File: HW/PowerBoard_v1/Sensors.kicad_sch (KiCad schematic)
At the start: 46 parts, among them U3 MCP9700AT-ETT, U4 PAMC1350DWVR, U5 PAMC1350DWVR, U6 PAMC1350DWVR, U7 PAMC1350DWVR, U8 3v3 ISO DC/DC

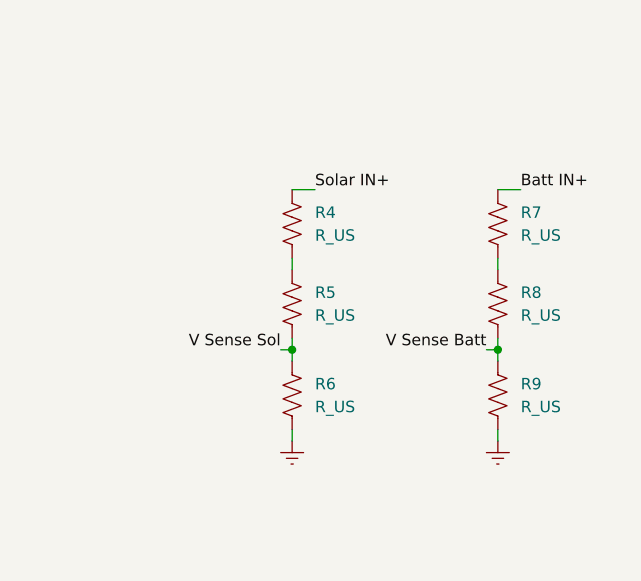
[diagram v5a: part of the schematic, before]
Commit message: added resistor values for voltage sense
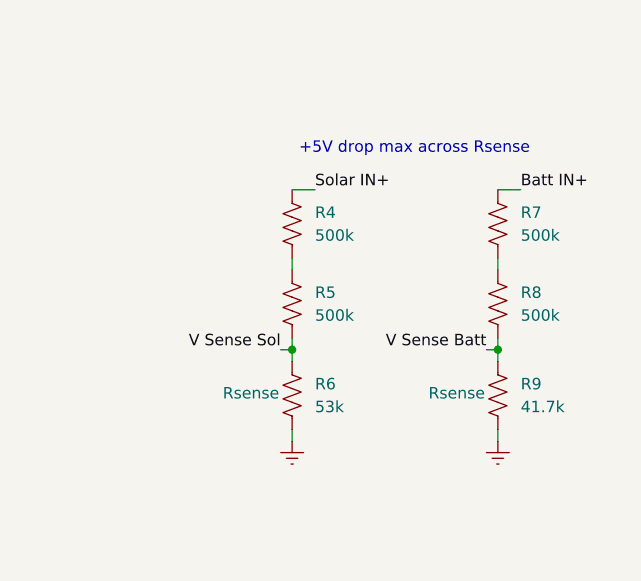
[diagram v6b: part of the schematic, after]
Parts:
- R4, R5, R7, R8: value R_US -> 500k; footprint (none) -> Resistor_SMD:R_0603_1608Metric_Pad0.98x0.95mm_HandSolder
- R6: value R_US -> 53k; footprint (none) -> Resistor_SMD:R_0603_1608Metric_Pad0.98x0.95mm_HandSolder; MPN (none) -> RN73H1JTTD5302D100; Note (none) -> Rsense
- R9: value R_US -> 41.7k; footprint (none) -> Resistor_SMD:R_0603_1608Metric_Pad0.98x0.95mm_HandSolder; MPN (none) -> RN73R1JTTD4172F10; Note (none) -> Rsense
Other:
- note added: "+5V drop max across Rsense"

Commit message: finished schematic
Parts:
- R10, R11: value R_US -> 0.75; footprint (none) -> Package_TO_SOT_SMD:TO-263-2_TabPin1; MPN (none) -> PWR263S-35-R750F; Note (none) -> Isense
- R6, R9: Note Rsense -> Vsense
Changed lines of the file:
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@@
 	)
 	(symbol
+		(lib_id "device:R_US")
+		(at 248.92 93.98 90)
+		(unit 1)
+		(exclude_from_sim no)
+		(in_bom yes)
+		(on_board yes)
+		(dnp no)
+		(property "Reference" "R11"
+			(at 248.92 91.186 90)
+			(effects
+				(font
+					(size 1.27 1.27)
+				)
+			)
+		)
+		(property "Value" "0.75"
+			(at 248.92 96.266 90)
+			(effects
+				(font
+					(size 1.27 1.27)
+				)
+			)
+		)
+		(property "Footprint" "Package_TO_SOT_SMD:TO-263-2_TabPin1"
+			(at 249.174 92.964 90)
+			(effects
+				(font
+					(size 1.27 1.27)
+				)
+				(hide yes)
+			)
+		)
+		(property "Datasheet" "https://www.bourns.com/docs/Product-Datasheets/PWR263S-35.pdf"
+			(at 248.92 93.98 0)
+			(effects
+				(font
+					(size 1.27 1.27)
+				)
+				(hide yes)
+			)
+		)
+		(property "Description" "Resistor, US symbol"
+			(at 248.92 93.98 0)
+			(effects
+				(font
+					(size 1.27 1.27)
+				)
+				(hide yes)
+			)
+		)
+		(property "MPN" "PWR263S-35-R750F "
+			(at 248.92 93.98 90)
+			(effects
+				(font
+					(size 1.27 1.27)
+				)
+				(hide yes)
+			)
+		)
+		(property "Note" "Isense"
+			(at 243.332 96.012 90)
+			(effects
+				(font
+					(size 1.27 1.27)
+				)
+			)
+		)
+		(pin "2"
+		)
+		(pin "1"
+		)
+		(instances
+			(project "power_v1"
+				(path "/1e1b062d-fad0-427c-a622-c5b8a80b5268/f37b00a5-62bb-47d6-b18e-0a47b6349fc3"
+					(reference "R11")
+					(unit 1)
+				)
+			)
+		)
+	)
+	(symbol
 		(lib_id "power:Earth")
 		(at 170.18 93.98 0)
@@
 			)
 		)
-		(property "Note" "Rsense"
+		(property "Note" "Vsense"
 			(at 231.648 54.356 0)
 			(effects
@@
 		(on_board yes)
 		(dnp no)
-		(fields_autoplaced yes)
 		(property "Reference" "R10"
-			(at 248.92 77.47 90)
+			(at 248.92 81.026 90)
 			(effects
 				(font
@@
 			)
 		)
-		(property "Value" "R_US"
-			(at 248.92 80.01 90)
+		(property "Value" "0.75"
+			(at 248.92 86.106 90)
 			(effects
 				(font
@@
 			)
 		)
-		(property "Footprint" ""
+		(property "Footprint" "Package_TO_SOT_SMD:TO-263-2_TabPin1"
 			(at 249.174 82.804 90)
 			(effects
@@
 			)
 		)
-		(property "Datasheet" "~"
+		(property "Datasheet" "https://www.bourns.com/docs/Product-Datasheets/PWR263S-35.pdf"
 			(at 248.92 83.82 0)
 			(effects
@@
 			)
 		)
+		(property "MPN" "PWR263S-35-R750F "
+			(at 248.92 83.82 90)
+			(effects
+				(font
+					(size 1.27 1.27)
+				)
+				(hide yes)
+			)
+		)
+		(property "Note" "Isense"
+			(at 243.332 85.852 90)
+			(effects
+				(font
+					(size 1.27 1.27)
+				)
+			)
+		)
 		(pin "2"
 		)
@@
 			)
 		)
-		(property "Note" "Rsense"
+		(property "Note" "Vsense"
 			(at 254.508 54.356 0)
 			(effects
@@
 					(unit 1)
 				)
-			)
-		)
-	)
-	(symbol
-		(lib_id "device:R_US")
-		(at 248.92 93.98 90)
-		(unit 1)
-		(exclude_from_sim no)
-		(in_bom yes)
-		(on_board yes)
-		(dnp no)
-		(fields_autoplaced yes)
-		(property "Reference" "R11"
-			(at 248.92 87.63 90)
-			(effects
-				(font
-					(size 1.27 1.27)
-				)
-			)
-		)
-		(property "Value" "R_US"
-			(at 248.92 90.17 90)
-			(effects
-				(font
-					(size 1.27 1.27)
-				)
-			)
-		)
-		(property "Footprint" ""
-			(at 249.174 92.964 90)
-			(effects
-				(font
-					(size 1.27 1.27)
-				)
-				(hide yes)
-			)
-		)
-		(property "Datasheet" "~"
-			(at 248.92 93.98 0)
-			(effects
-				(font
-					(size 1.27 1.27)
-				)
-				(hide yes)
-			)
-		)
-		(property "Description" "Resistor, US symbol"
-			(at 248.92 93.98 0)
-			(effects
-				(font
-					(size 1.27 1.27)
-				)
-				(hide yes)
-			)
-		)
-		(pin "2"
-		)
-		(pin "1"
-		)
-		(instances
-			(project "power_v1"
-				(path "/1e1b062d-fad0-427c-a622-c5b8a80b5268/f37b00a5-62bb-47d6-b18e-0a47b6349fc3"
-					(reference "R11")
-					(unit 1)
-				)
